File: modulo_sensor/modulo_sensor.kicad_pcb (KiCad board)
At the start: 2 copper layers, 112.4 x 40.1 mm, 33 parts, among them J1 Conn_01x08_Pin, U1 74HC14DR2G

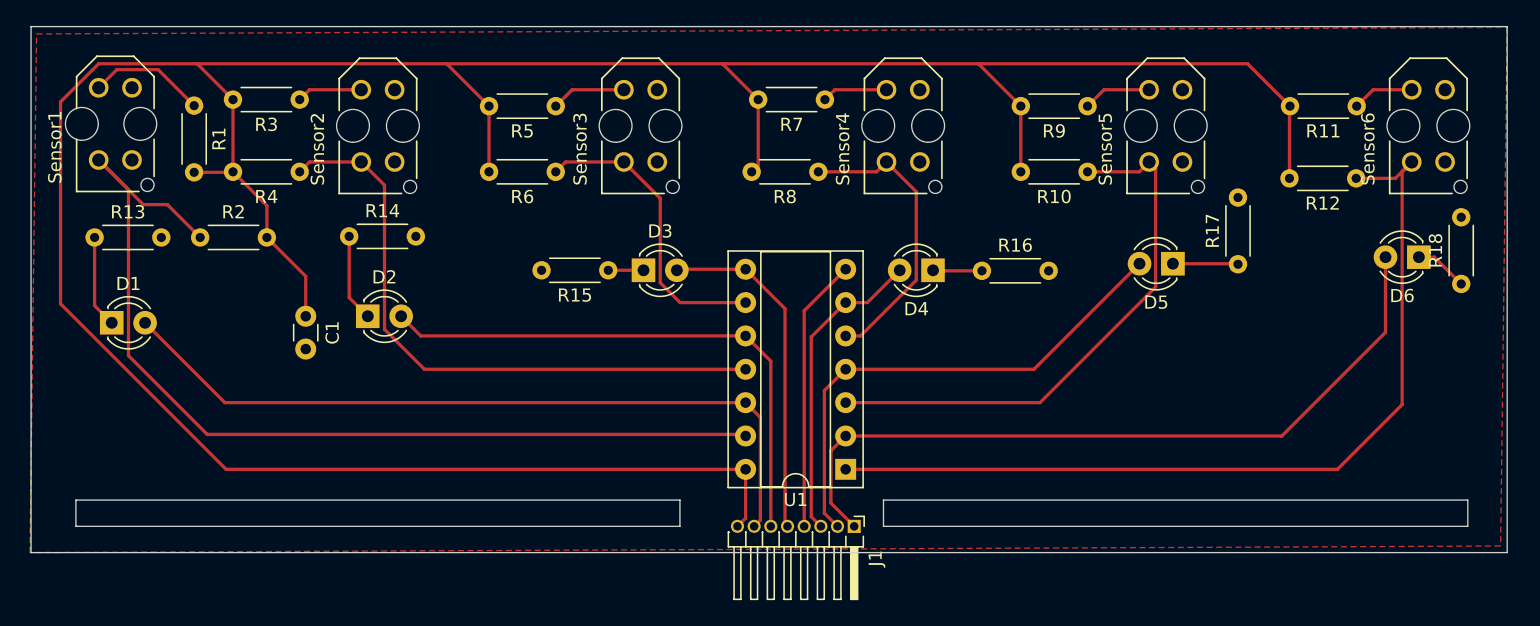
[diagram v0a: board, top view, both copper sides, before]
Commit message: refactor: Cambio los footprints de todas las resistencias THT por SMD
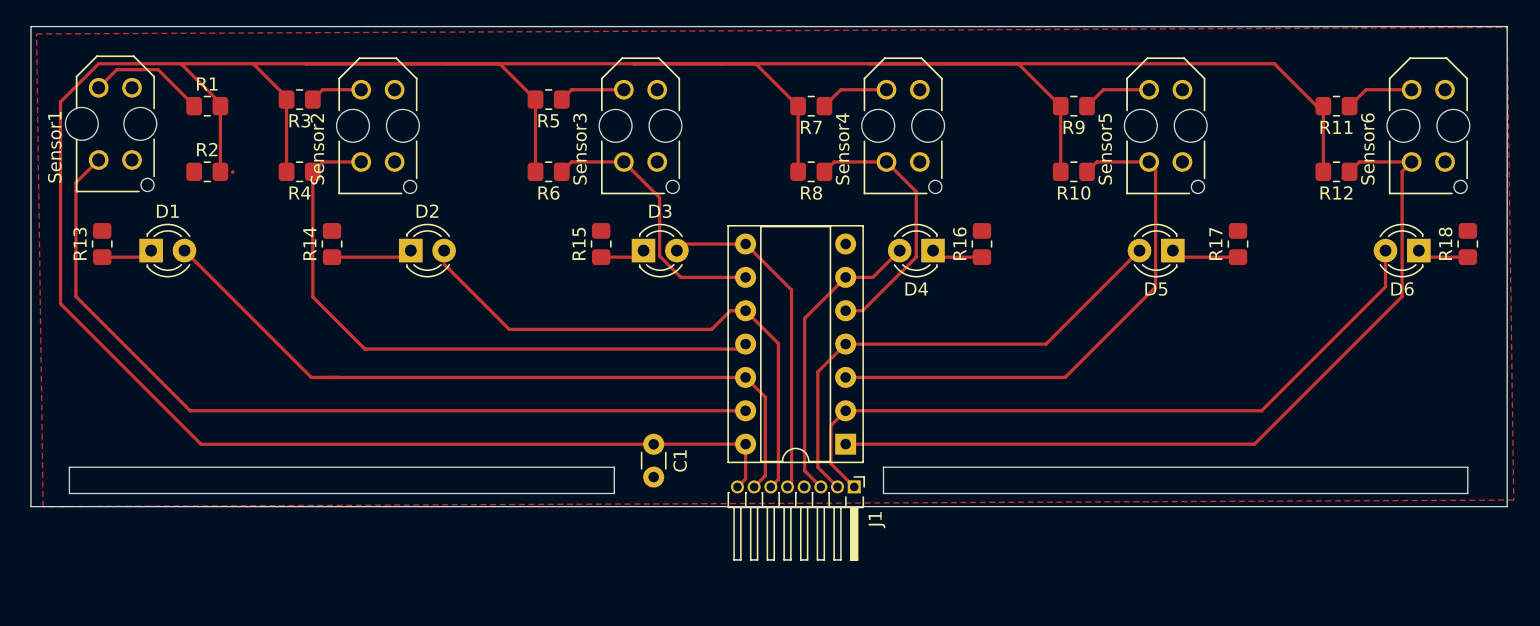
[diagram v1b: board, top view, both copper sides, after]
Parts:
- R1, R10, R11, R12, R13, R14, R15, R16, R17, R18, R2, R3, R4, R5, R6, R7, R8, R9: footprint Resistor_THT:R_Axial_DIN0204_L3.6mm_D1.6mm_P5.08mm_Horizontal -> Resistor_SMD:R_0805_2012Metric_Pad1.20x1.40mm_HandSolder
- moved C1 28.2 mm to (116.0, 59.8)
- moved D1 6.26 mm to (77.7, 45.0)
- moved D2 5.98 mm to (97.5, 45.0)
- moved R2 5.03 mm to (82.0, 39.0)
- moved R18 3.08 mm to (178.0, 44.5)
- moved J1 3.00 mm to (131.3, 63.0)
- moved R15 2.07 mm to (112.0, 44.5), turned to 90 degrees
- moved R16 2.04 mm to (141.0, 44.5), turned to 90 degrees
- moved U1 1.92 mm to (130.6, 59.7)
- moved R12 1.58 mm to (168.0, 39.0)
- moved R17 1.54 mm to (160.5, 44.5)
- moved R11 1.54 mm to (168.0, 34.0)
- moved D3 1.50 mm to (115.2, 45.0)
- moved D4 1.50 mm to (137.3, 45.0)
- moved R14 1.43 mm to (91.5, 44.5), turned to 90 degrees
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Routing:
- net vcc: track 233.4 -> 261.8 mm
- net GND: track 20.9 -> 0.62 mm
- net /Sensor1: track 75.5 -> 65.7 mm
- net /Sensor6: track 68.0 -> 62.7 mm
- net /Led_Sensor6: track 58.2 -> 54.8 mm
- net Net-(D1-K): track 7.04 -> 3.93 mm
- net /Sensor3: track 23.0 -> 20.6 mm
- net /Sensor4: track 22.6 -> 20.3 mm
- net /Led_Sensor2: track 42.2 -> 40.3 mm
- net /Led_Sensor1: track 58.3 -> 56.8 mm
- net /Sensor2: track 47.2 -> 48.3 mm
- net /Led_Sensor5: track 38.8 -> 37.7 mm
- net Net-(R3-Pad1): track 5.00 -> 4.00 mm
- net /Led_Sensor4: track 23.6 -> 22.7 mm
- net /Sensor5: track 42.0 -> 41.2 mm
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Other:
- board size 112.4 x 40.1 mm -> 112.4 x 36.6 mm

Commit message: refactor: Reduzco la distancia entre los sensores centrales dentro de 20mm
Ahora hay 18,07mm de centro a centro en los sensores 3 y 4
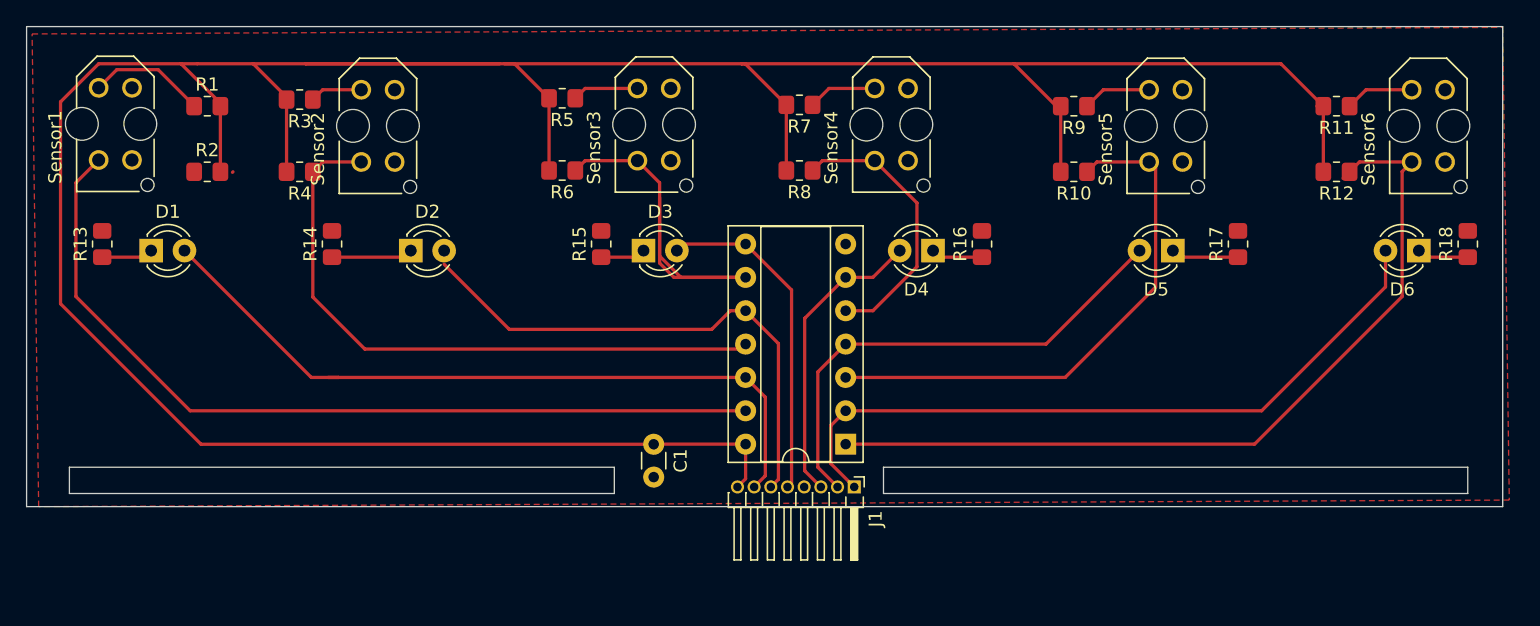
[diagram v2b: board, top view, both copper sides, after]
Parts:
- moved R5 1.03 mm to (109.0, 33.4)
- moved R6 1.03 mm to (109.0, 38.9)
- moved Sensor3 1.03 mm to (116.0, 35.4)
- moved R7 0.91 mm to (127.1, 33.9)
- moved R8 0.91 mm to (127.1, 38.9)
- moved Sensor4 0.91 mm to (134.1, 35.4)
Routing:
- net vcc: track 261.8 -> 242.6 mm
- net /Sensor3: track 20.6 -> 32.2 mm
- net /Sensor4: track 20.3 -> 21.3 mm
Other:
- outline, holes or cut-outs redrawn

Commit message: fix: Arreglo algunas conexiones sueltas y relleno B.Cu con GND
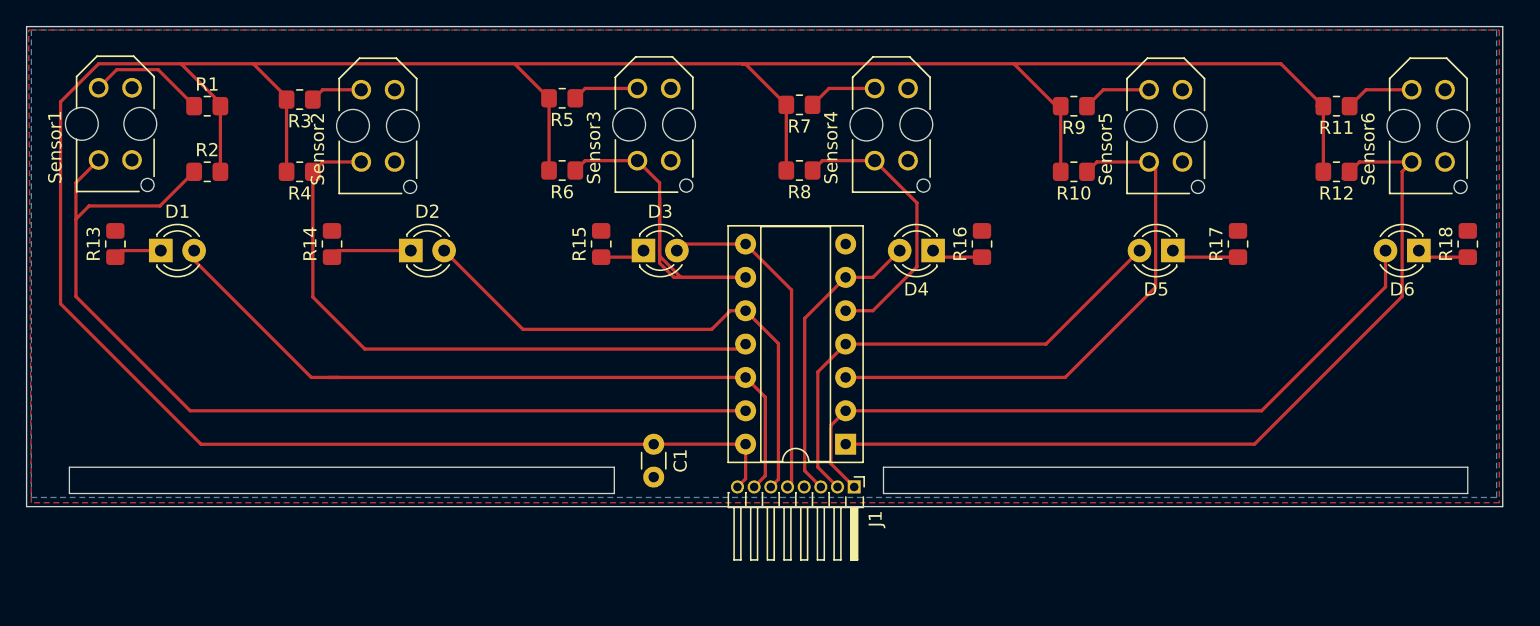
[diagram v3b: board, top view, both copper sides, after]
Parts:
- moved R13 1.00 mm to (75.0, 44.5)
- moved D1 0.73 mm to (78.5, 45.0)
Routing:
- net vcc: track 242.6 -> 227.2 mm
- net /Sensor1: track 65.7 -> 76.2 mm
- net Net-(D2-K): track 6.21 -> 6.91 mm
- added copper zone on B.Cu, net GND

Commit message: fix: Reruteo las pistas que pasan entre los leds, y alejo las pistas entre sí
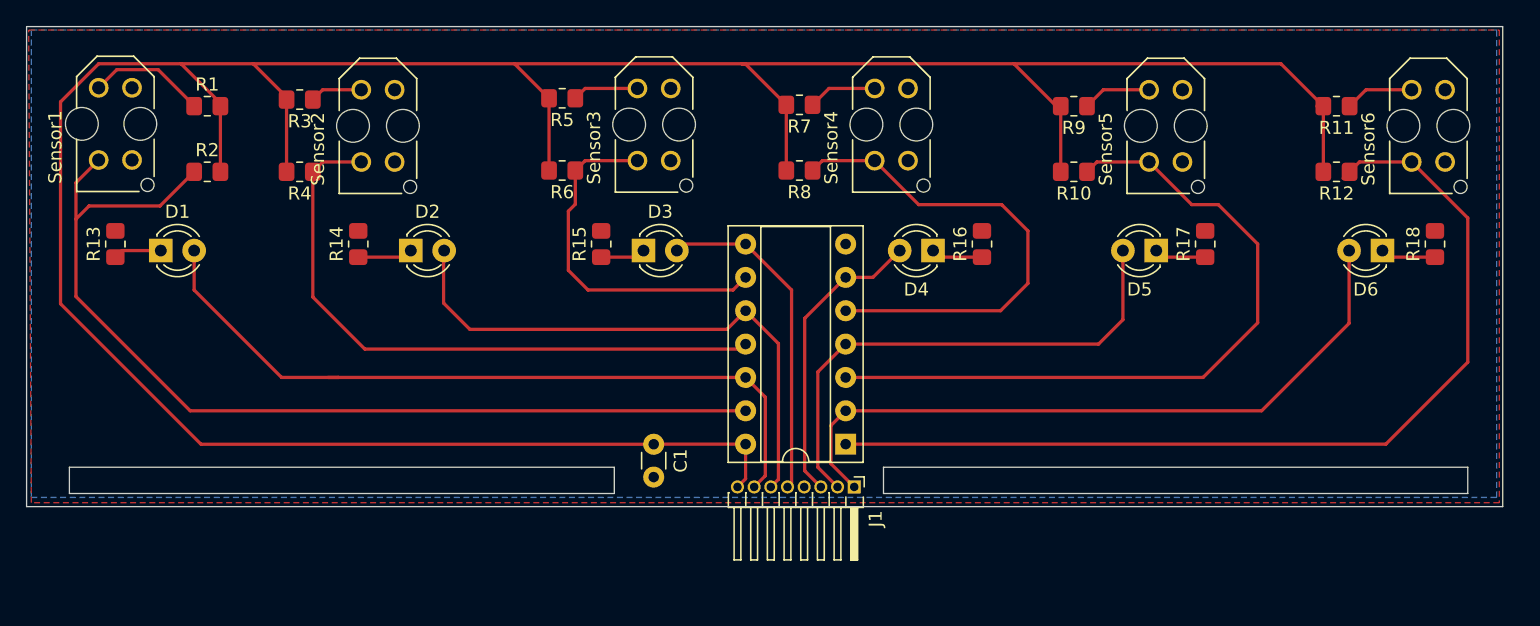
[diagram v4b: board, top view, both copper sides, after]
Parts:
- moved D6 2.78 mm to (171.5, 45.0)
- moved R17 2.50 mm to (158.0, 44.5)
- moved R18 2.50 mm to (175.5, 44.5)
- moved R14 2.00 mm to (93.5, 44.5)
- moved D5 1.26 mm to (154.3, 45.0)
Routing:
- net /Sensor4: track 21.3 -> 37.7 mm
- net /Sensor5: track 41.2 -> 55.0 mm
- net /Sensor6: track 62.7 -> 72.1 mm
- net /Sensor3: track 32.2 -> 27.4 mm
- net Net-(D2-K): track 6.91 -> 4.21 mm
- net /Led_Sensor2: track 40.7 -> 43.2 mm
- net /Led_Sensor5: track 37.7 -> 39.5 mm
- net /Led_Sensor1: track 56.5 -> 57.9 mm
- net Net-(D5-K): track 5.17 -> 3.93 mm
- net /Led_Sensor6: track 54.8 -> 53.6 mm
